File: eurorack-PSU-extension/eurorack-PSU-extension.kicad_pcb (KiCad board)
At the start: 2 copper layers, 100 x 40 mm, 14 parts, among them J1 Screw_Terminal_01x03, J10 Screw_Terminal_01x03, J2 Conn_02x05_Top_Bottom, J3 Conn_02x05_Top_Bottom, J4 Conn_02x05_Top_Bottom, J5 Conn_02x05_Top_Bottom, J6 Conn_02x05_Top_Bottom, J7 Conn_02x05_Top_Bottom, M3 MountingHole_3.2mm_M3_ISO7380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

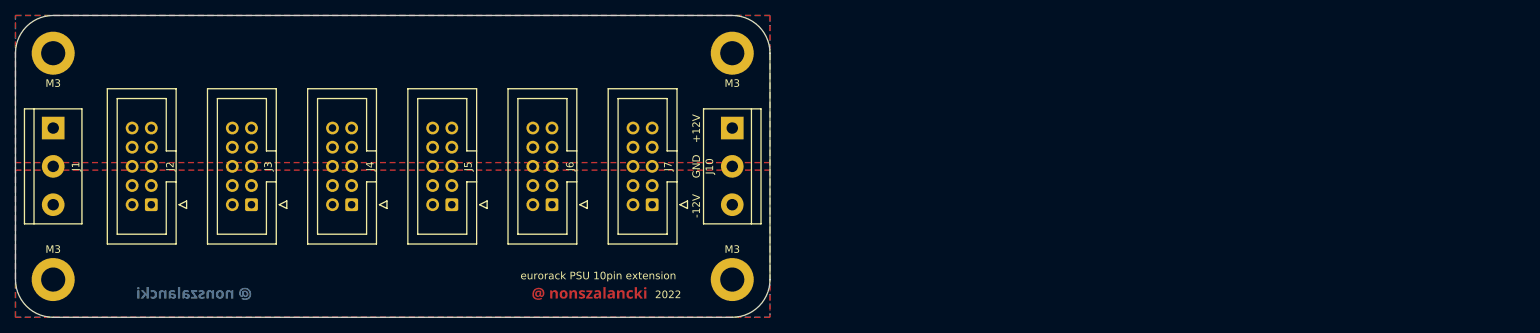
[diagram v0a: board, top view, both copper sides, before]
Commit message: silkscreen changes
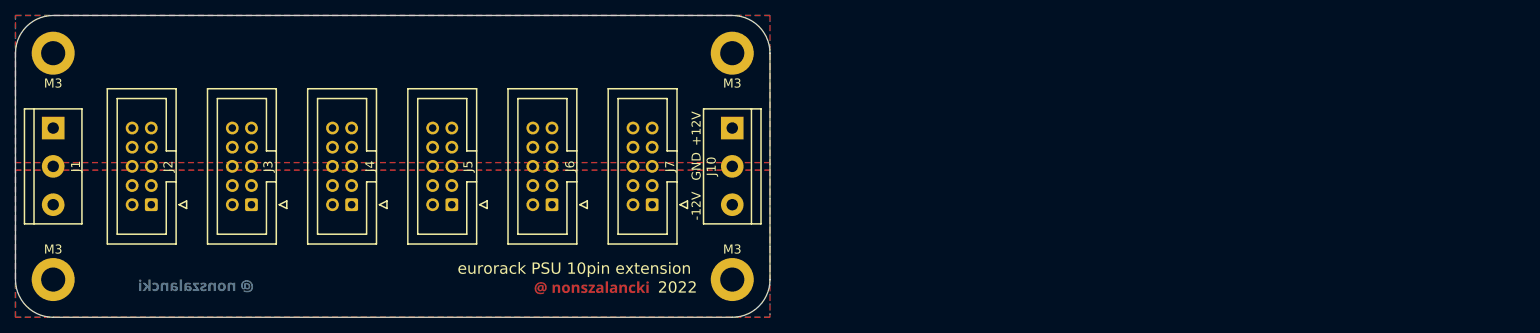
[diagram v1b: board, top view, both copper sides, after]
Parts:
- moved svg2mod 1.03 mm to (62.5, 68.0)
- moved svg2mod 0.81 mm to (99.8, 68.2)

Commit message: added protection diode for 78xx & 79xx, corrected orientation of some parts
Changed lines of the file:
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@@
       (disableapertmacros false)
       (usegerberextensions true)
-      (usegerberattributes true)
-      (usegerberadvancedattributes true)
-      (creategerberjobfile true)
+      (usegerberattributes false)
+      (usegerberadvancedattributes false)
+      (creategerberjobfile false)
       (svguseinch false)
       (svgprecision 6)
-      (excludeedgelayer false)
+      (excludeedgelayer true)
       (plotframeref false)
       (viasonmask false)
@@
       (psa4output false)
       (plotreference true)
-      (plotvalue true)
+      (plotvalue false)
       (plotinvisibletext false)
       (sketchpadsonfab false)
@@
       (drillshape 0)
       (scaleselection 1)
-      (outputdirectory "gbrl/")
+      (outputdirectory "C:/Users/marci/Documents/KiCAD/6.0/projects/Eurorack/Power supply/eurorack-PSU/eurorack-PSU-extension/gerber/")
     )
   )
@@
     (fp_line (start -3.18 -4.1) (end -2.18 -5.1) (layer "F.Fab") (width 0.1))
     (fp_line (start -1.98 7.13) (end -1.98 7.13) (layer "F.Fab") (width 0.1))
-    (pad "1" thru_hole roundrect (at 0 0 180) (size 1.7 1.7) (drill 1) (layers *.Cu *.Mask) (roundrect_rratio 0.147059)
+    (pad "1" thru_hole roundrect (at 0 0 180) (size 1.7 1.7) (drill 1) (layers *.Cu *.Mask) (roundrect_rratio 0.1470588235)
       (net 3 "-12V") (pinfunction "Pin_1") (pintype "passive"))
     (pad "2" thru_hole circle (at 2.54 0 180) (size 1.7 1.7) (drill 1) (layers *.Cu *.Mask)
@@
     (fp_line (start -1.98 -3.91) (end 4.52 -3.91) (layer "F.Fab") (width 0.1))
     (fp_line (start -1.98 14.07) (end -1.98 7.13) (layer "F.Fab") (width 0.1))
-    (pad "1" thru_hole roundrect (at 0 0 180) (size 1.7 1.7) (drill 1) (layers *.Cu *.Mask) (roundrect_rratio 0.147059)
+    (pad "1" thru_hole roundrect (at 0 0 180) (size 1.7 1.7) (drill 1) (layers *.Cu *.Mask) (roundrect_rratio 0.1470588235)
       (net 3 "-12V") (pinfunction "Pin_1") (pintype "passive"))
     (pad "2" thru_hole circle (at 2.54 0 180) (size 1.7 1.7) (drill 1) (layers *.Cu *.Mask)
@@
     (fp_line (start -3.18 -4.1) (end -2.18 -5.1) (layer "F.Fab") (width 0.1))
     (fp_line (start -1.98 7.13) (end -3.18 7.13) (layer "F.Fab") (width 0.1))
-    (pad "1" thru_hole roundrect (at 0 0 180) (size 1.7 1.7) (drill 1) (layers *.Cu *.Mask) (roundrect_rratio 0.147059)
+    (pad "1" thru_hole roundrect (at 0 0 180) (size 1.7 1.7) (drill 1) (layers *.Cu *.Mask) (roundrect_rratio 0.1470588235)
       (net 3 "-12V") (pinfunction "Pin_1") (pintype "passive"))
     (pad "2" thru_hole circle (at 2.54 0 180) (size 1.7 1.7) (drill 1) (layers *.Cu *.Mask)
@@
     (fp_line (start -3.18 3.03) (end -1.98 3.03) (layer "F.Fab") (width 0.1))
     (fp_line (start 4.52 14.07) (end -1.98 14.07) (layer "F.Fab") (width 0.1))
-    (pad "1" thru_hole roundrect (at 0 0 180) (size 1.7 1.7) (drill 1) (layers *.Cu *.Mask) (roundrect_rratio 0.147059)
+    (pad "1" thru_hole roundrect (at 0 0 180) (size 1.7 1.7) (drill 1) (layers *.Cu *.Mask) (roundrect_rratio 0.1470588235)
       (net 3 "-12V") (pinfunction "Pin_1") (pintype "passive"))
     (pad "2" thru_hole circle (at 2.54 0 180) (size 1.7 1.7) (drill 1) (layers *.Cu *.Mask)
@@
     (fp_line (start -1.98 3.03) (end -1.98 -3.91) (layer "F.Fab") (width 0.1))
     (fp_line (start 4.52 14.07) (end -1.98 14.07) (layer "F.Fab") (width 0.1))
-    (pad "1" thru_hole roundrect (at 0 0 180) (size 1.7 1.7) (drill 1) (layers *.Cu *.Mask) (roundrect_rratio 0.147059)
+    (pad "1" thru_hole roundrect (at 0 0 180) (size 1.7 1.7) (drill 1) (layers *.Cu *.Mask) (roundrect_rratio 0.1470588235)
       (net 3 "-12V") (pinfunction "Pin_1") (pintype "passive"))
     (pad "2" thru_hole circle (at 2.54 0 180) (size 1.7 1.7) (drill 1) (layers *.Cu *.Mask)
@@
     (fp_line (start -1.98 7.13) (end -1.98 7.13) (layer "F.Fab") (width 0.1))
     (fp_line (start -1.98 3.03) (end -1.98 -3.91) (layer "F.Fab") (width 0.1))
-    (pad "1" thru_hole roundrect (at 0 0 180) (size 1.7 1.7) (drill 1) (layers *.Cu *.Mask) (roundrect_rratio 0.147059)
+    (pad "1" thru_hole roundrect (at 0 0 180) (size 1.7 1.7) (drill 1) (layers *.Cu *.Mask) (roundrect_rratio 0.1470588235)
       (net 3 "-12V") (pinfunction "Pin_1") (pintype "passive"))
     (pad "2" thru_hole circle (at 2.54 0 180) (size 1.7 1.7) (drill 1) (layers *.Cu *.Mask)

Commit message: PSU extension rework
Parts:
- removed the J6 at (102.1, 58.1)
- removed the J7 at (115.4, 58.1)
- removed the M3 at (126.0, 68.0)
- removed the M3 at (126.0, 38.0)
- removed the svg2mod at (99.8, 68.2)
- removed the svg2mod at (62.5, 68.0)
- added J1: Screw_Terminal_01x03, TerminalBlock_XINYA:TerminalBlock_XINYA_XY301-1x3-P5.00mm, F.Cu at (39.7, 45.5)
- added J10: Screw_Terminal_01x03, TerminalBlock_XINYA:TerminalBlock_XINYA_XY301-1x3-P5.00mm, F.Cu at (222.1, 60.5)
- added J2: Conn_02x05_Top_Bottom, Connector_IDC:IDC-Header_2x05_P2.54mm_Vertical, F.Cu at (56.7, 58.1)
- added J3: Conn_02x05_Top_Bottom, Connector_IDC:IDC-Header_2x05_P2.54mm_Vertical, F.Cu at (78.2, 58.1)
- added M3: MountingHole_3.2mm_M3_ISO7380_Pad, MountingHole:MountingHole_3.2mm_M3_ISO7380_Pad, F.Cu at (226.0, 68.0)
- added M3: MountingHole_3.2mm_M3_ISO7380_Pad, MountingHole:MountingHole_3.2mm_M3_ISO7380_Pad, F.Cu at (131.0, 38.0)
- added M3: MountingHole_3.2mm_M3_ISO7380_Pad, MountingHole:MountingHole_3.2mm_M3_ISO7380_Pad, F.Cu at (131.0, 68.0)
- added M3: MountingHole_3.2mm_M3_ISO7380_Pad, MountingHole:MountingHole_3.2mm_M3_ISO7380_Pad, F.Cu at (226.0, 38.0)
- added svg2mod: G***, Signature:@ nonszalancki 2-sans-serif-bold-nomask, F.Cu at (198.2, 68.9)
- added svg2mod: G***, Signature:@ nonszalancki 2-sans-serif-bold-nomask, B.Cu at (63.1, 68.6)
- J4: renamed from J1; value Screw_Terminal_01x03 -> Conn_02x05_Top_Bottom; footprint TerminalBlock:TerminalBlock_bornier-3_P5.08mm -> Connector_IDC:IDC-Header_2x05_P2.54mm_Vertical
- J9: renamed from J10; value Screw_Terminal_01x03 -> Conn_02x05_Top_Bottom; footprint TerminalBlock:TerminalBlock_bornier-3_P5.08mm -> Connector_IDC:IDC-Header_2x05_P2.54mm_Vertical
- moved J8 96.5 mm to (185.3, 58.1)
- moved J7 88.3 mm to (163.9, 58.1)
- moved J9 80.8 mm to (206.8, 58.1), turned to 180 degrees
- moved J6 80.2 mm to (142.4, 58.1)
- moved J5 72.0 mm to (121.0, 58.1)
- moved J4 64.4 mm to (99.6, 58.1), turned to 180 degrees
- renumbered J2 to J5, J3 to J6, J4 to J7, J5 to J8
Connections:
- J4 pad 1: +12V -> -12V
- J4 pad 2: GND -> -12V
- J4 pad 3: -12V -> GND
- J9 pad 2: GND -> -12V
- J9 pad 3: +12V -> GND
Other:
- board size 100 x 40 mm -> 200 x 40 mm

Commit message: minor part placement changes
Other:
- board text added: "JLCJLCJLCJLC"
